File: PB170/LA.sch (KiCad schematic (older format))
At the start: 7 parts

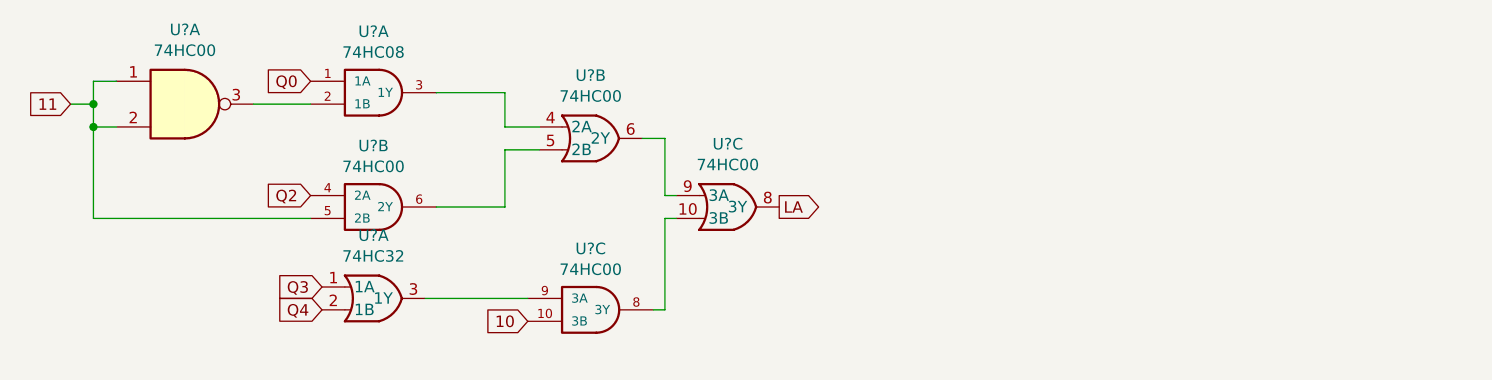
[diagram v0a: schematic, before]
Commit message: added LEDs, mby we could try to start routing
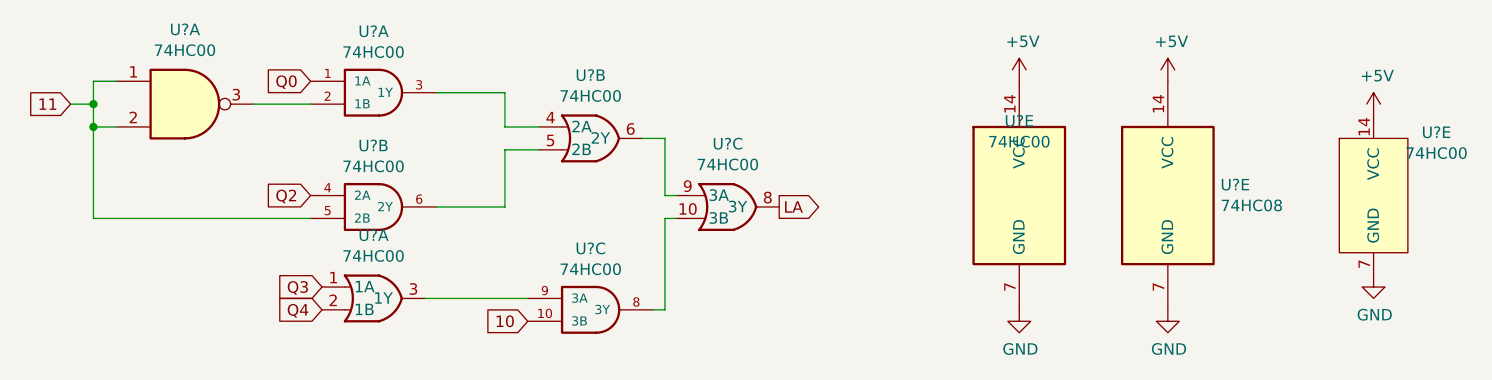
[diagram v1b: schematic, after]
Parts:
- added U?: 74HC00, Package_SO:TSSOP-14_4.4x5mm_P0.65mm, symbol PB170:74HC32
- added U?: 74HC08, Housings_SOIC:SOIC-14_3.9x8.7mm_Pitch1.27mm, symbol PB170:74HC08
- added U?: 74HC00, Package_SO:TSSOP-14_4.4x5mm_P0.65mm, symbol 74xx:74HC00
- U?: value 74HC08 -> 74HC00; footprint Housings_SOIC:SOIC-14_3.9x8.7mm_Pitch1.27mm -> Package_SO:TSSOP-14_4.4x5mm_P0.65mm
- U?: value 74HC32 -> 74HC00; footprint Housings_SOIC:SOIC-14_3.9x8.7mm_Pitch1.27mm -> Package_SO:TSSOP-14_4.4x5mm_P0.65mm
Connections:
- new net +5V: U?.14 (VCC), U?.14 (VCC), U?.14 (VCC)
- new net GND: U?.7 (GND), U?.7 (GND), U?.7 (GND)
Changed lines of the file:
@@
 P 5200 3300
 F 0 "U?" H 5225 3567 50  0000 C CNN
-F 1 "74HC08" H 5225 3476 50  0000 C CNN
-F 2 "Housings_SOIC:SOIC-14_3.9x8.7mm_Pitch1.27mm" H 5200 3300 50  0001 C CNN
-F 3 "https://datasheet.lcsc.com/szlcsc/Nexperia-74HC08D-653_C5593.pdf" H 5200 3300 50  0001 C CNN
+F 1 "74HC00" H 5225 3476 50  0000 C CNN
+F 2 "Package_SO:TSSOP-14_4.4x5mm_P0.65mm" H 5200 3300 50  0001 C CNN
+F 3 "https://datasheet.lcsc.com/szlcsc/Texas-Instruments-TI-SN74HC00PWR_C6807.pdf" H 5200 3300 50  0001 C CNN
 F 4 "C5593" H 5200 3300 50  0001 C CNN "LCSC"
 	1    5200 3300
@@
 P 5250 4200
 F 0 "U?" H 5225 4475 50  0000 C CNN
-F 1 "74HC32" H 5225 4384 50  0000 C CNN
-F 2 "Housings_SOIC:SOIC-14_3.9x8.7mm_Pitch1.27mm" H 4700 4400 50  0001 C CNN
-F 3 "https://datasheet.lcsc.com/szlcsc/Nexperia-74HC32D-653_C5632.pdf" H 4700 4400 50  0001 C CNN
+F 1 "74HC00" H 5225 4384 50  0000 C CNN
+F 2 "Package_SO:TSSOP-14_4.4x5mm_P0.65mm" H 4700 4400 50  0001 C CNN
+F 3 "https://datasheet.lcsc.com/szlcsc/Texas-Instruments-TI-SN74HC00PWR_C6807.pdf" H 4700 4400 50  0001 C CNN
 F 4 "C5632" H 5250 4200 50  0001 C CNN "LCSC"
 	1    5250 4200
@@
 Text GLabel 7000 3800 2    50   Output ~ 0
 LA
+Wire Wire Line
+	4950 3350 4700 3350
+Wire Wire Line
+	4100 3250 4000 3250
+Wire Wire Line
+	4000 3250 4000 3350
+Wire Wire Line
+	4000 3450 4100 3450
+Wire Wire Line
+	4000 3350 3900 3350
+Connection ~ 4000 3350
+Wire Wire Line
+	4000 3350 4000 3450
+Text GLabel 3900 3350 0    50   Input ~ 0
+11
+Wire Wire Line
+	4000 3450 4000 3850
+Wire Wire Line
+	4000 3850 4950 3850
+Connection ~ 4000 3450
+Text GLabel 5900 4300 0    50   Input ~ 0
+10
+$Comp
+L PB170:74HC08 U?
+U 5 1 602CA937
+P 8700 3750
+F 0 "U?" H 8930 3796 50  0000 L CNN
+F 1 "74HC08" H 8930 3705 50  0000 L CNN
+F 2 "Housings_SOIC:SOIC-14_3.9x8.7mm_Pitch1.27mm" H 8700 3750 50  0001 C CNN
+F 3 "https://datasheet.lcsc.com/szlcsc/Nexperia-74HC08D-653_C5593.pdf" H 8700 3750 50  0001 C CNN
+F 4 "C5593" H 8700 3750 50  0001 C CNN "LCSC"
+	5    8700 3750
+	1    0    0    -1
+$EndComp
+$Comp
+L power:GND #PWR?
+U 1 1 6026EC5A
+P 9600 4100
+F 0 "#PWR?" H 9600 3850 50  0001 C CNN
+F 1 "GND" H 9605 3927 50  0000 C CNN
+F 2 "" H 9600 4100 50  0001 C CNN
+F 3 "" H 9600 4100 50  0001 C CNN
+	1    9600 4100
+	1    0    0    -1
+$EndComp
+$Comp
+L power:+5V #PWR?
+U 1 1 6026F7D9
+P 8700 3250
+F 0 "#PWR?" H 8700 3100 50  0001 C CNN
+F 1 "+5V" H 8715 3423 50  0000 C CNN
+F 2 "" H 8700 3250 50  0001 C CNN
+F 3 "" H 8700 3250 50  0001 C CNN
+	1    8700 3250
+	1    0    0    -1
+$EndComp
+$Comp
+L PB170:74HC32 U?
+U 5 1 602993DA
+P 9900 3750
+F 0 "U?" H 9875 4025 50  0000 C CNN
+F 1 "74HC00" H 9875 3934 50  0000 C CNN
+F 2 "Package_SO:TSSOP-14_4.4x5mm_P0.65mm" H 9350 3950 50  0001 C CNN
+F 3 "https://datasheet.lcsc.com/szlcsc/Texas-Instruments-TI-SN74HC00PWR_C6807.pdf" H 9350 3950 50  0001 C CNN
+F 4 "C5632" H 9900 3750 50  0001 C CNN "LCSC"
+	5    9900 3750
+	1    0    0    -1
+$EndComp
+$Comp
+L power:+5V #PWR?
+U 1 1 6029D2A2
+P 9600 3400
+F 0 "#PWR?" H 9600 3250 50  0001 C CNN
+F 1 "+5V" H 9615 3573 50  0000 C CNN
+F 2 "" H 9600 3400 50  0001 C CNN
+F 3 "" H 9600 3400 50  0001 C CNN
+	1    9600 3400
+	1    0    0    -1
+$EndComp
+$Comp
+L power:GND #PWR?
+U 1 1 602A59E1
+P 8700 4250
+F 0 "#PWR?" H 8700 4000 50  0001 C CNN
+F 1 "GND" H 8705 4077 50  0000 C CNN
+F 2 "" H 8700 4250 50  0001 C CNN
+F 3 "" H 8700 4250 50  0001 C CNN
+	1    8700 4250
+	1    0    0    -1
+$EndComp
 $Comp
 L 74xx:74HC00 U?
@@
 	1    0    0    -1
 $EndComp
-Wire Wire Line
-	4950 3350 4700 3350
-Wire Wire Line
-	4100 3250 4000 3250
-Wire Wire Line
-	4000 3250 4000 3350
-Wire Wire Line
-	4000 3450 4100 3450
-Wire Wire Line
-	4000 3350 3900 3350
-Connection ~ 4000 3350
-Wire Wire Line
-	4000 3350 4000 3450
-Text GLabel 3900 3350 0    50   Input ~ 0
-11
-Wire Wire Line
-	4000 3450 4000 3850
-Wire Wire Line
-	4000 3850 4950 3850
-Connection ~ 4000 3450
-Text GLabel 5900 4300 0    50   Input ~ 0
-10
+$Comp
+L 74xx:74HC00 U?
+U 5 1 603563F9
+P 8050 3750
+F 0 "U?" H 8050 4075 50  0000 C CNN
+F 1 "74HC00" H 8050 3984 50  0000 C CNN
+F 2 "Package_SO:TSSOP-14_4.4x5mm_P0.65mm" H 8050 3750 50  0001 C CNN
+F 3 "https://datasheet.lcsc.com/szlcsc/Texas-Instruments-TI-SN74HC00PWR_C6807.pdf" H 8050 3750 50  0001 C CNN
+F 4 "C6807" H 8050 3750 50  0001 C CNN "LCSC"
+	5    8050 3750
+	1    0    0    -1
+$EndComp
+$Comp
+L power:+5V #PWR?
+U 1 1 6035ED67
+P 8050 3250
+F 0 "#PWR?" H 8050 3100 50  0001 C CNN
+F 1 "+5V" H 8065 3423 50  0000 C CNN
+F 2 "" H 8050 3250 50  0001 C CNN
+F 3 "" H 8050 3250 50  0001 C CNN
+	1    8050 3250
+	1    0    0    -1
+$EndComp
+$Comp
+L power:GND #PWR?
+U 1 1 6035F7C5
+P 8050 4250
+F 0 "#PWR?" H 8050 4000 50  0001 C CNN
+F 1 "GND" H 8055 4077 50  0000 C CNN
+F 2 "" H 8050 4250 50  0001 C CNN
+F 3 "" H 8050 4250 50  0001 C CNN
+	1    8050 4250
+	1    0    0    -1
+$EndComp
 $EndSCHEMATC
